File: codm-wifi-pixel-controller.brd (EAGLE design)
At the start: 59 x 25.5 mm, 50 parts, among them U1 AP62XXX-TSOT26, U2 REG710NA-5/250, U3 SN74AHCT125PWR, U5 ESP32-WROOM-32D

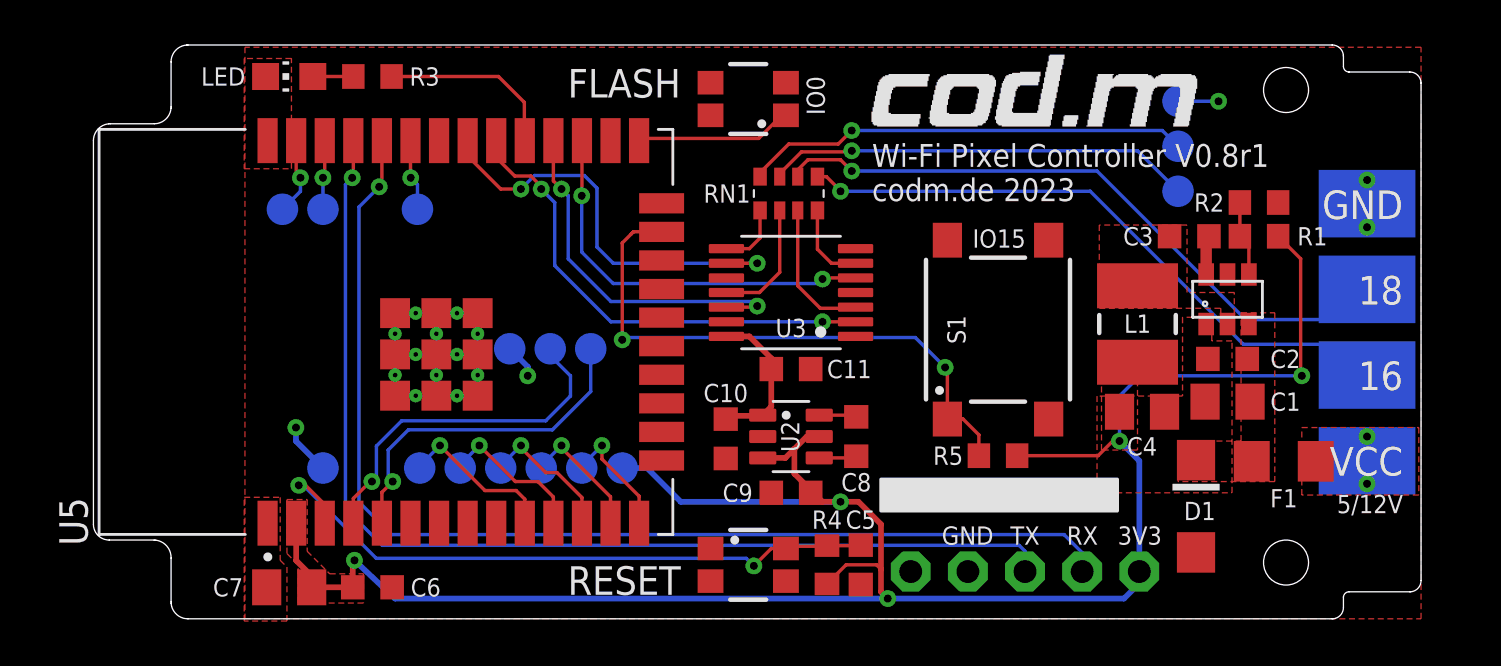
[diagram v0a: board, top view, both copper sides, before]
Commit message: better fiducials
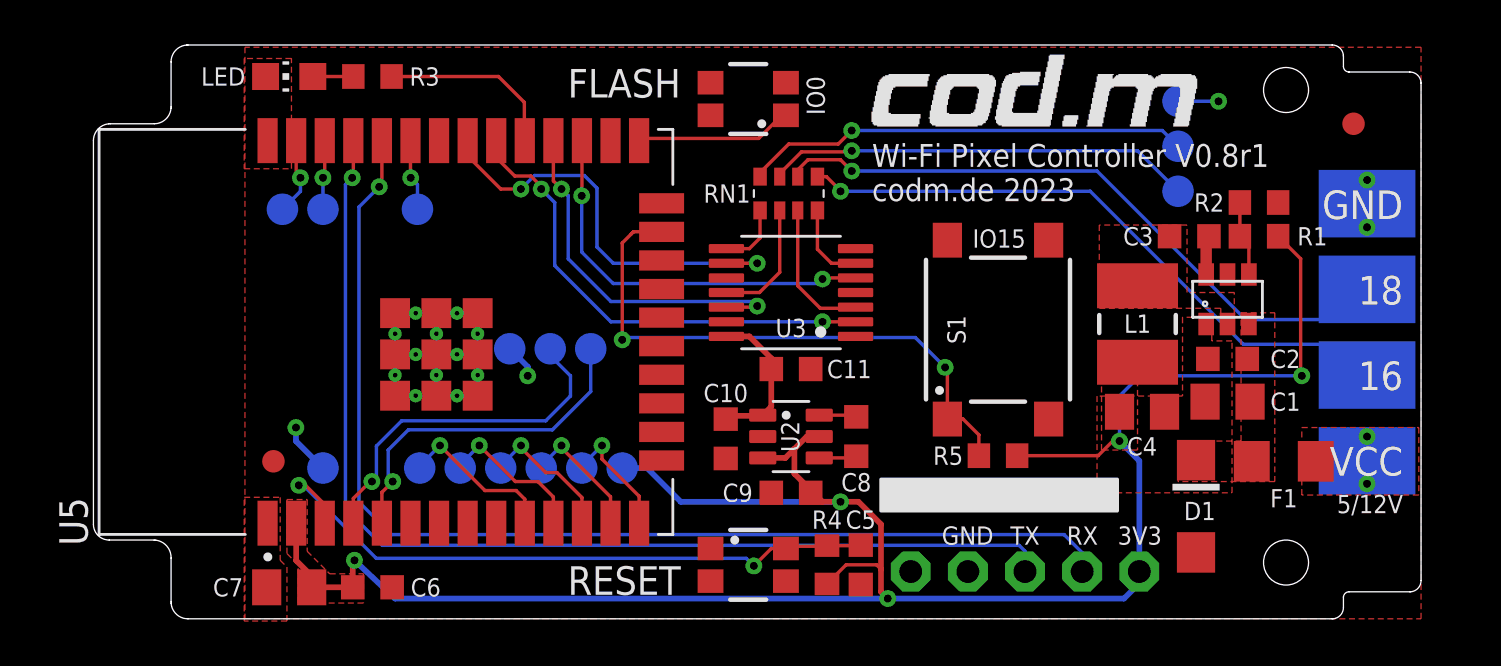
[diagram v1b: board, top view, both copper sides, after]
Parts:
- added FD1, FD2: FIDUCIAL1X2, SparkFun-Aesthetics:FIDUCIAL-1X2
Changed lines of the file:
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@@
 <text x="58.2" y="7" size="1.27" layer="25" ratio="20" align="center-right">VCC</text>
 <text x="29.5" y="17.1" size="1.4224" layer="26" ratio="12" rot="MR0" align="center">Wi-Fi Pixel Controller V0.8r1</text>
-<circle x="8" y="7" radius="1" width="0" layer="29"/>
-<circle x="56" y="22" radius="1" width="0" layer="29"/>
 <text x="58.2" y="5.1" size="0.8128" layer="25" font="vector" align="center-right">5/12V</text>
 <circle x="53" y="2.5" radius="2.05" width="0.1524" layer="52"/>
@@
 <attribute name="VALUE" x="28" y="3.25" size="1.27" layer="27" rot="R90"/>
 </element>
+<element name="FD1" library="SparkFun-Aesthetics" library_urn="urn:adsk.eagle:library:507" package="FIDUCIAL-1X2" package3d_urn="urn:adsk.eagle:package:37108/1" value="FIDUCIAL1X2" x="8" y="7" smashed="yes"/>
+<element name="FD2" library="SparkFun-Aesthetics" library_urn="urn:adsk.eagle:library:507" package="FIDUCIAL-1X2" package3d_urn="urn:adsk.eagle:package:37108/1" value="FIDUCIAL1X2" x="56" y="22" smashed="yes"/>
 </elements>
 <signals>
